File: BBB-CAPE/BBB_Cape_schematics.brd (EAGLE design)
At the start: 160 x 100 mm, 84 parts, among them IC1 EEPROM-I2CSMD, SW2 219-02

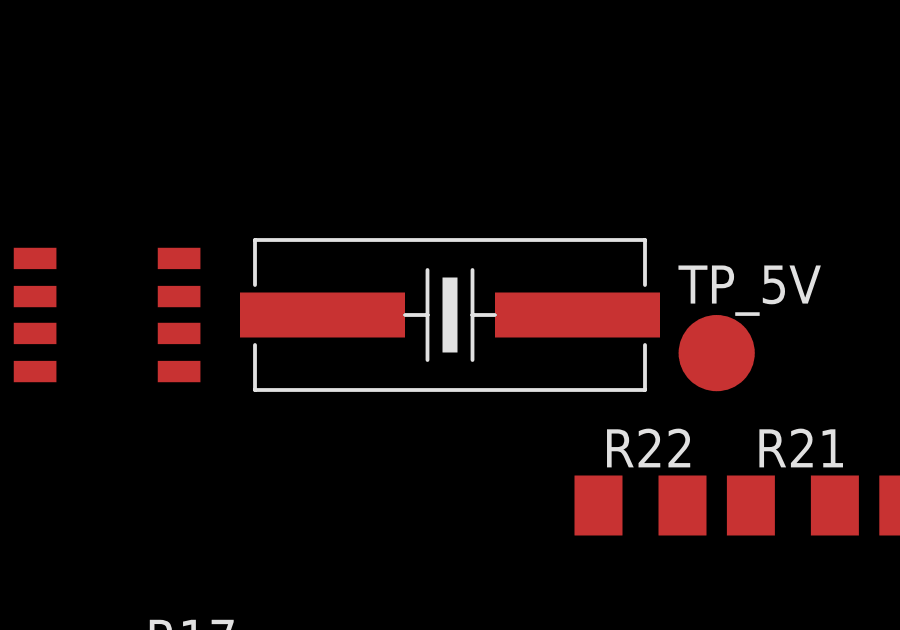
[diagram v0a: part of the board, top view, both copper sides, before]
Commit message: Change +5V signal to 5V signal in BBB_Cape_schematics.sch and Update 12MHz crystal package in BBB_Cape_schematics.brd
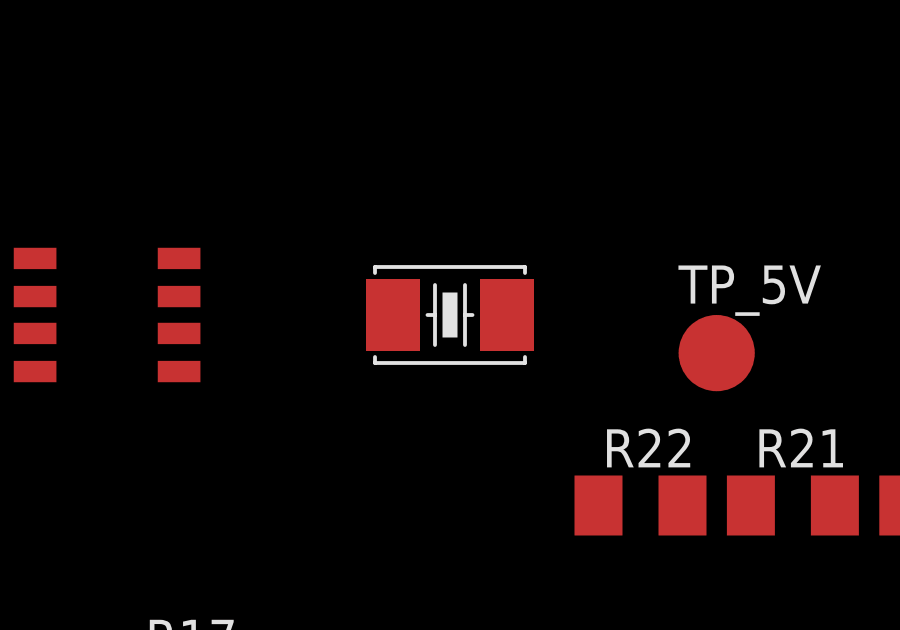
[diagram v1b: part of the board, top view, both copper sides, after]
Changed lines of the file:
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@@
 <wire x1="-118.24" y1="205.74" x2="-97.66" y2="205.74" width="0" layer="19" extent="1-1"/>
-</signal>
-<signal name="N$19">
-<contactref element="U$12" pad="P$1"/>
-<contactref element="R16" pad="2"/>
-<contactref element="R15" pad="1"/>
-<contactref element="C9" pad="2"/>
-<wire x1="-64.45" y1="216.02" x2="-46.86" y2="205.74" width="0" layer="19" extent="1-1"/>
-<wire x1="-100.46" y1="205.74" x2="-64.45" y2="216.02" width="0" layer="19" extent="1-1"/>
-<wire x1="-104.01" y1="205.74" x2="-100.46" y2="205.74" width="0" layer="19" extent="1-1"/>
 </signal>
 <signal name="+5V/2">
@@
 <contactref element="U$23" pad="P$1"/>
 <contactref element="U$10" pad="1"/>
-<wire x1="-147.76" y1="212.09" x2="-85.62" y2="218.145" width="0" layer="19" extent="1-1"/>
+<wire x1="-145.41" y1="212.09" x2="-85.62" y2="218.145" width="0" layer="19" extent="1-1"/>
 </signal>
 <signal name="N$28">
 <contactref element="U$23" pad="P$2"/>
 <contactref element="U$10" pad="8"/>
-<wire x1="-139.26" y1="212.09" x2="-82.02" y2="218.145" width="0" layer="19" extent="1-1"/>
+<wire x1="-141.61" y1="212.09" x2="-82.02" y2="218.145" width="0" layer="19" extent="1-1"/>
 </signal>
 <signal name="N$29">
@@
 <wire x1="-125.6" y1="205.74" x2="-85.62" y2="216.845" width="0" layer="19" extent="1-1"/>
 </signal>
+<signal name="N$19">
+<contactref element="R16" pad="2"/>
+<contactref element="U$12" pad="P$1"/>
+<contactref element="C9" pad="2"/>
+<contactref element="R15" pad="1"/>
+<wire x1="-64.45" y1="216.02" x2="-46.86" y2="205.74" width="0" layer="19" extent="1-1"/>
+<wire x1="-100.46" y1="205.74" x2="-64.45" y2="216.02" width="0" layer="19" extent="1-1"/>
+<wire x1="-104.01" y1="205.74" x2="-100.46" y2="205.74" width="0" layer="19" extent="1-1"/>
+</signal>
 </signals>

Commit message: Place components and Route for -5V, 2.5V supply in BBB_Cape_schematics.brd and Change +5V to 5V in BBB_schematics.sch
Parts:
- moved R17 314.0 mm to (86.4, -4.60)
- moved JP5 308.2 mm to (97.8, -14.0), turned to 180 degrees
- moved C4 304.3 mm to (76.2, -36.8)
- moved R22 300.9 mm to (77.5, -5.08)
- moved U$19 295.6 mm to (87.6, 43.2), turned to 180 degrees
- moved R12 293.2 mm to (83.8, -33.0), turned to 90 degrees
- moved JP1 286.8 mm to (77.5, -14.0)
- moved R26 284.5 mm to (86.4, -8.41)
- moved R10 284.2 mm to (80.0, -20.3)
- moved C22 281.8 mm to (83.8, -27.9), turned to 90 degrees
- moved R11 280.4 mm to (71.1, -30.5), turned to 270 degrees
- moved U$23 279.4 mm to (80.0, 44.5)
- moved JP3 278.4 mm to (87.6, -14.0)
- moved C17 276.5 mm to (76.2, -34.3)
- moved R9 276.4 mm to (74.9, -20.3)
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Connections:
- net +5V: no longer C12.1, U$22.P$5
- net 5V: now also C12.1, U$22.P$5
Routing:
- net 5V: track 30.0 -> 88.6 mm
- net GND: track 10.2 -> 42.0 mm, vias 2 -> 7
- net N$26: track 0.00 -> 13.9 mm
- net +5V/2: track 0.00 -> 11.8 mm
- net N$25: track 0.00 -> 11.5 mm
- net N$21: track 23.3 -> 14.3 mm
- net N$9: track 2.24 -> 9.11 mm
- net N$6: track 5.64 -> 3.73 mm
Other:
- board size 160 x 100 mm -> 135.9 x 163.5 mm
